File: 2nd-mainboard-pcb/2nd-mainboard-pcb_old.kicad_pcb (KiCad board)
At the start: 4 copper layers, 99 x 97.5 mm, 132 parts, among them J1 PJ-082BH, J10 Servo Motor BL Touch, J11 T3, J12 Steckverbinder_Male_Fans, J13 Steckverbinder_Female_Leistung, J14 FAN3, J15 Steckverbinder_Female_Motoren, J16 ISP, J18 Quartz, J19 T2, J2 Fan_12/5V_Regelung, J20 T2, J21 T2, J22 T3, J23 Conn_01x04_Socket, J24 Steckverbinder_Male_Leistung, J3 Fan_12/5V_Regelung, J4 FAN0, J5 FAN1, J6 FAN2, J7 Stepper Motor, J8 Servo Motor SM, J9 Microstepping, P1 USB_C_Receptacle_USB2.0_14P, U1 SQJ409EP-T1_GE3, U10 ATmega328PB-A, U12 MPU-6050, U2 SZ1SMB5927BT3G, U3 TPS56837HRPAR, U4 TPS565208, U5 FT232RL, U6 PTS647SM38SMTR2LFS, U7 TPM16050-S6TR, U8 RJK0456DPB-00-J5, U9 RJK0456DPB-00-J5, Y1 ECS-160-18-4X-CKM

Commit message: rearragned componentens
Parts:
- C13, C20, C21, C22, C23, C26, C27, C29, C30, C31, C32, C33, C35, C37, C38, C6, C7: footprint Capacitor_SMD:C_0603_1608Metric_Pad1.08x0.95mm_HandSolder -> Capacitor_SMD:C_0402_1005Metric_Pad0.74x0.62mm_HandSolder
- C2, C9: moved to F.Cu
- C28: footprint Capacitor_SMD:C_0603_1608Metric_Pad1.08x0.95mm_HandSolder -> Capacitor_SMD:C_0805_2012Metric_Pad1.18x1.45mm_HandSolder
- C8: moved to B.Cu
- R1, R10, R11, R12, R13, R14, R15, R16, R17, R22, R23, R24, R25, R4, R5, R6, R7, R8, R9: footprint Resistor_SMD:R_0603_1608Metric_Pad0.98x0.95mm_HandSolder -> Resistor_SMD:R_0402_1005Metric
- R2: footprint Resistor_SMD:R_0603_1608Metric_Pad0.98x0.95mm_HandSolder -> Resistor_SMD:R_0603_1608Metric
- R3: footprint Resistor_SMD:R_0603_1608Metric_Pad0.98x0.95mm_HandSolder -> Resistor_SMD:R_0402_1005Metric; moved to F.Cu
- moved G*** 86.9 mm to (139.7, 61.6)
- moved G*** 86.9 mm to (107.4, 82.0)
- moved R3 7.12 mm to (130.8, 114.9), turned to 180 degrees
- moved J16 3.43 mm to (142.4, 143.3), turned to 90 degrees
- moved C2 2.82 mm to (132.5, 117.1), turned to 180 degrees
- moved C30 2.30 mm to (66.3, 91.8)
- moved C31 2.30 mm to (75.6, 91.9)
- moved C32 2.30 mm to (81.2, 91.2)
- moved C33 2.30 mm to (81.2, 81.7)
- moved C36 2.30 mm to (75.8, 82.1)
- moved C37 2.30 mm to (76.6, 80.5)
- moved D5 2.30 mm to (89.9, 77.0)
- moved D6 2.30 mm to (89.8, 95.4)
- moved J12 2.30 mm to (74.5, 72.7)
- moved J14 2.30 mm to (83.6, 81.0)
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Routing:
- net GND: track 3.16 -> 708.6 mm, vias 0 -> 61
- net +5V_POW: track 0.00 -> 437.7 mm, vias 0 -> 13
- net AREF: track 0.00 -> 312.2 mm, vias 0 -> 22
- net +12V: track 0.00 -> 257.2 mm, vias 0 -> 11
- net MOSI: track 0.00 -> 201.5 mm, vias 0 -> 8
- net RESET: track 0.00 -> 121.8 mm, vias 0 -> 8
- net LED_MOT0: track 0.00 -> 118.0 mm, vias 0 -> 3
- net ADC0: track 0.00 -> 63.0 mm, vias 0 -> 5
- net ADC3: track 0.00 -> 61.0 mm, vias 0 -> 3
- net LED_MOT1: track 0.00 -> 58.9 mm, vias 0 -> 3
- net ADC2: track 0.00 -> 58.4 mm, vias 0 -> 3
- net ADC1: track 0.00 -> 57.7 mm, vias 0 -> 5
- net Quartz_1: track 0.00 -> 56.9 mm, vias 0 -> 1
- net STEP: track 0.00 -> 53.2 mm, vias 0 -> 2
- net Quartz_2: track 0.00 -> 49.0 mm
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- added copper zone on B.Cu, net GND
- added copper zone on F.Cu, net GND
- removed copper zone on In2.Cu, net +12V
- removed copper zone on In2.Cu, net +5V_POW
- removed copper zone on In1.Cu, net GND
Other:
- board size 99 x 97.5 mm -> 99 x 99 mm
- copper layers 4 -> 2

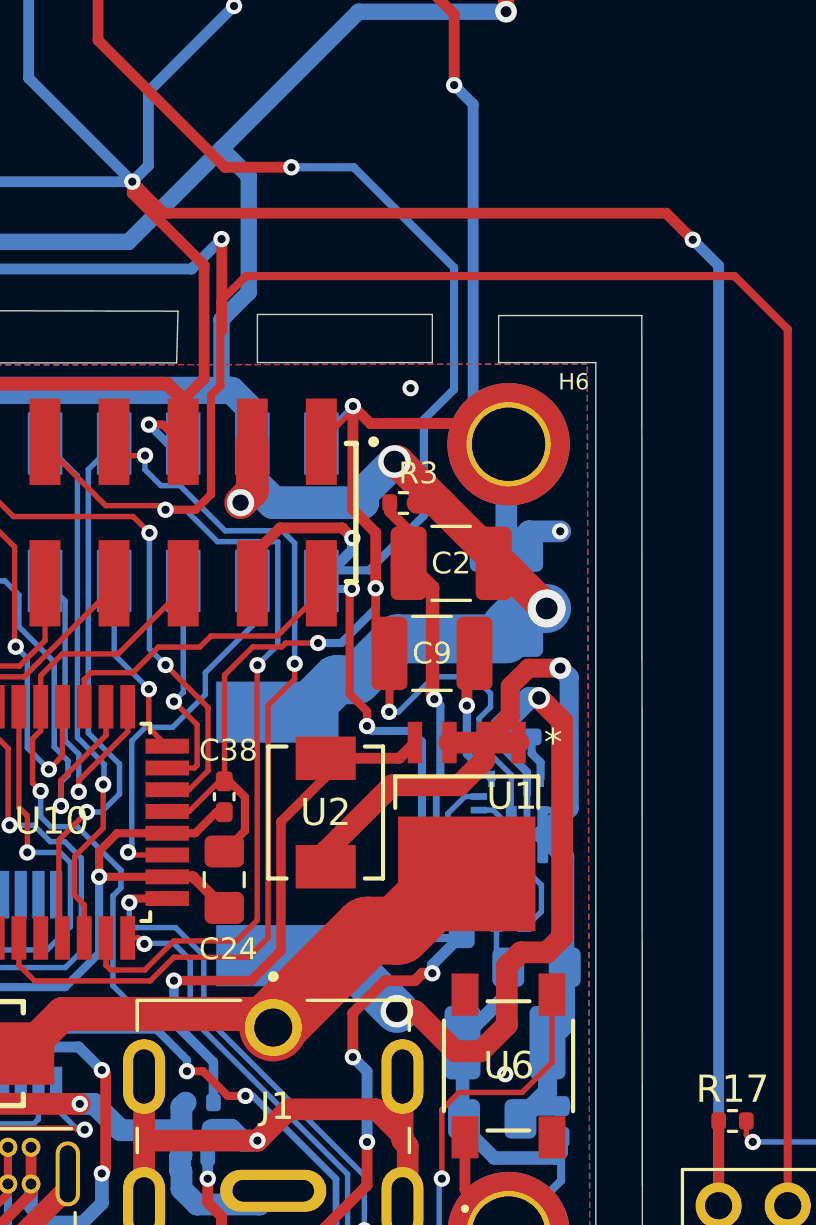
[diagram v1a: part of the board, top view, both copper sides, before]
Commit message: rearranged items a bit more, todo: fit item sizes to datasheets
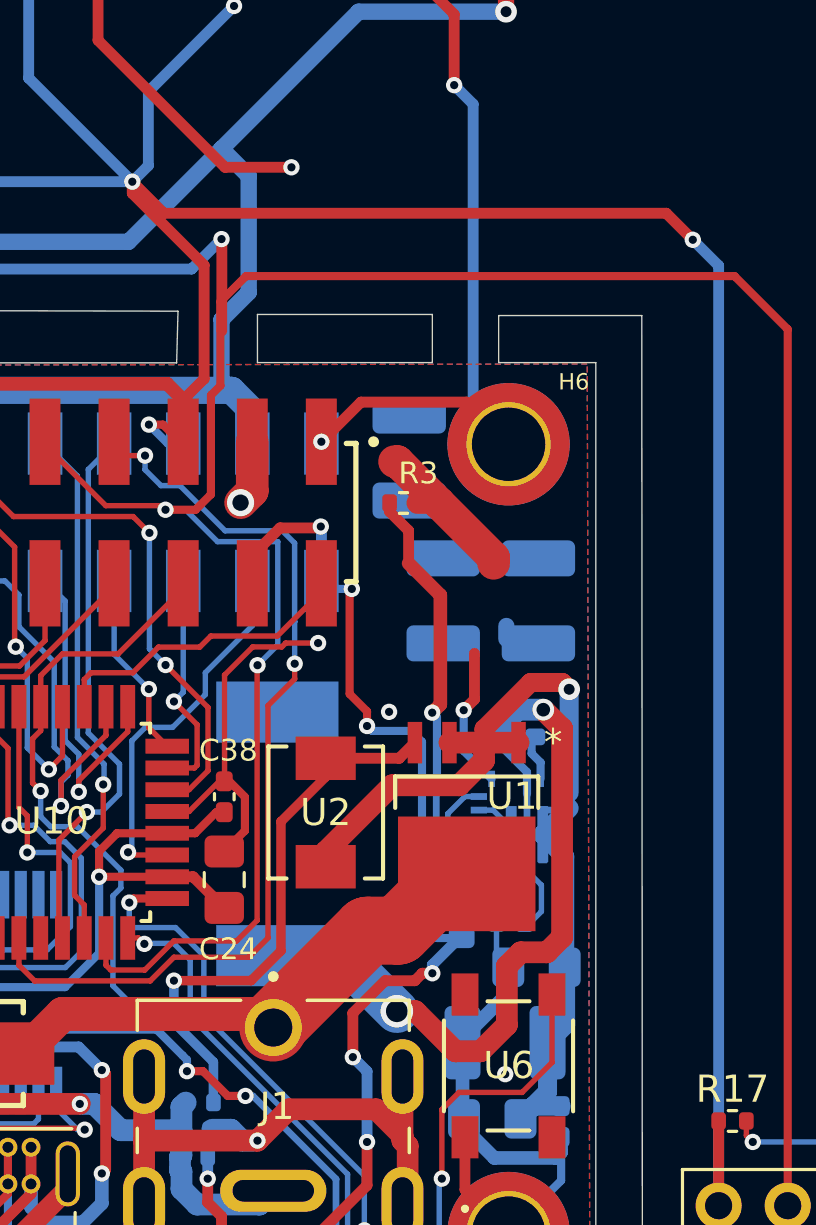
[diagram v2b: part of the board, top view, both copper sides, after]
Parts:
- C2, C9: moved to B.Cu
- moved C8 6.21 mm to (131.0, 113.2)
- moved C9 4.36 mm to (135.8, 118.5), turned to 90 degrees
- moved C2 1.41 mm to (132.2, 118.5), turned to -90 degrees
- moved C1 0.13 mm to (135.1, 123.5), turned to 0 degrees
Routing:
- net GND: track 708.6 -> 674.9 mm, vias 61 -> 58
- net AREF: track 312.2 -> 289.6 mm
- net +12V: track 257.2 -> 235.4 mm, vias 11 -> 9
- net PWR_IN_PROT: track 35.5 -> 33.9 mm
- net Net-(U3-SS): track 5.11 -> 5.68 mm
- net Net-(U3-SW): track 28.8 -> 28.3 mm
